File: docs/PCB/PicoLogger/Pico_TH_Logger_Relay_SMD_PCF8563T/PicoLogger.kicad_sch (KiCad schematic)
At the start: 62 parts, among them J1 Sensor, J2 LCD 16x2, J3 Additional connector, J4 K4_Output, J5 K3_Output, J6 K2_Output, J7 K1_Output, K1 G5Q-1, K2 G5Q-1, K3 G5Q-1, K4 G5Q-1, Q1 MMBT3904, Q2 MMBT3904, Q3 MMBT3904, Q4 MMBT3904, SW1 SW_Push, SW2 SW_Push, U1 LTV-817S, U2 LTV-817S, U3 LTV-817S, U4 LTV-817S, U5 PCF8563T, Y1 Crystal

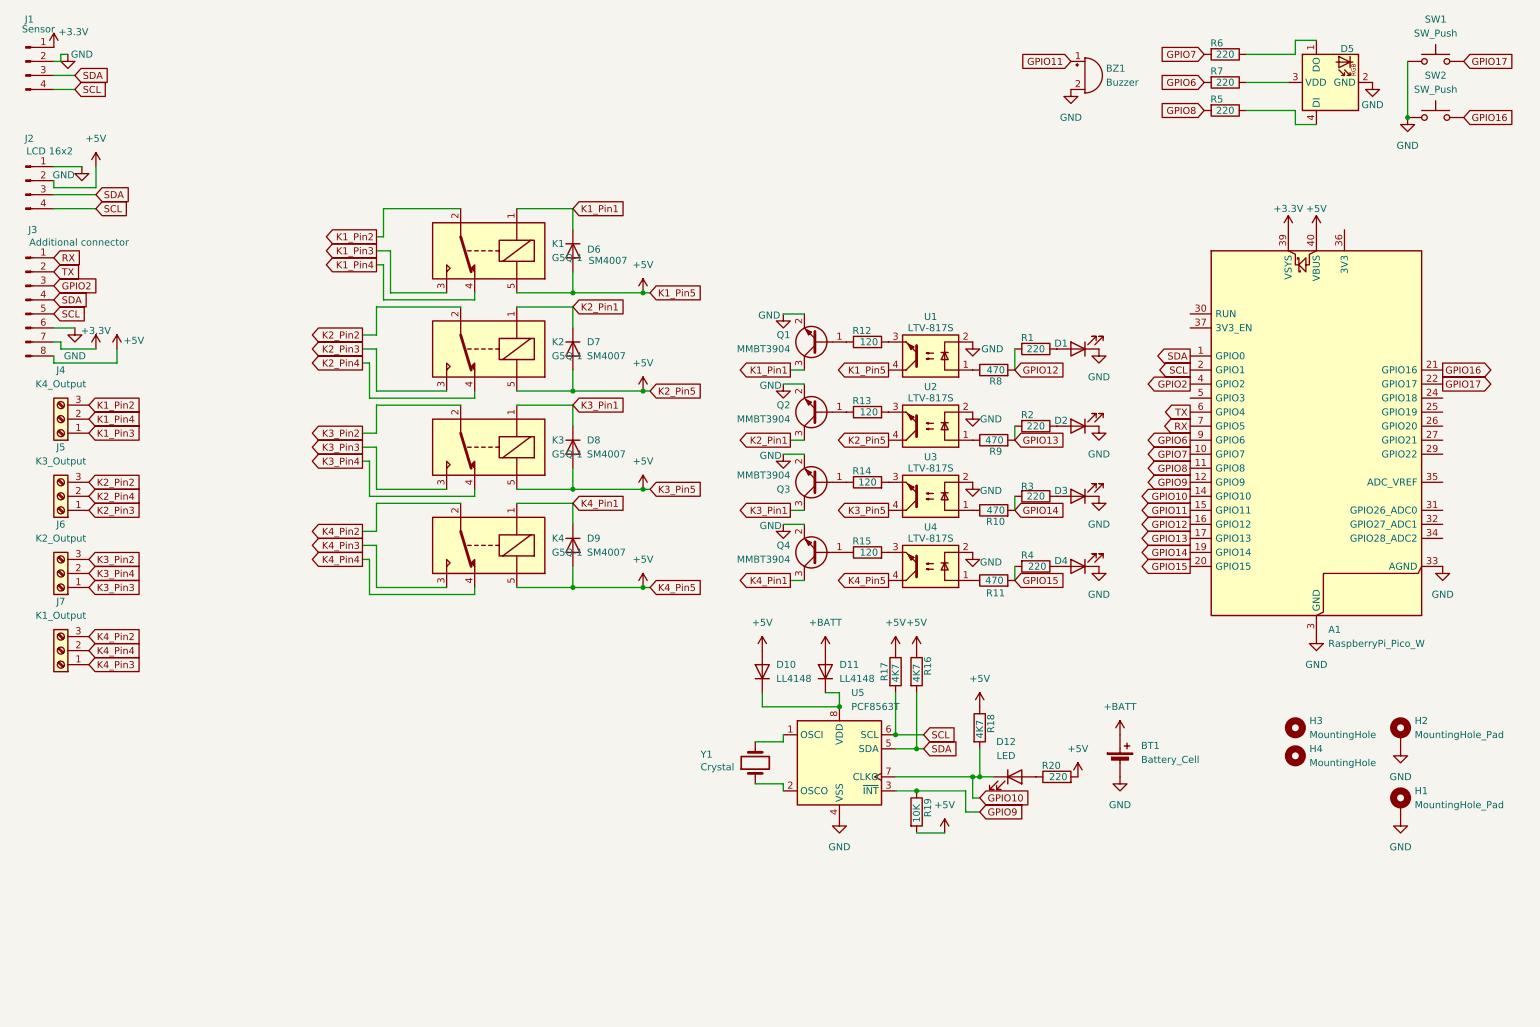
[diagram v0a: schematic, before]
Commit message: Logger docs updated.
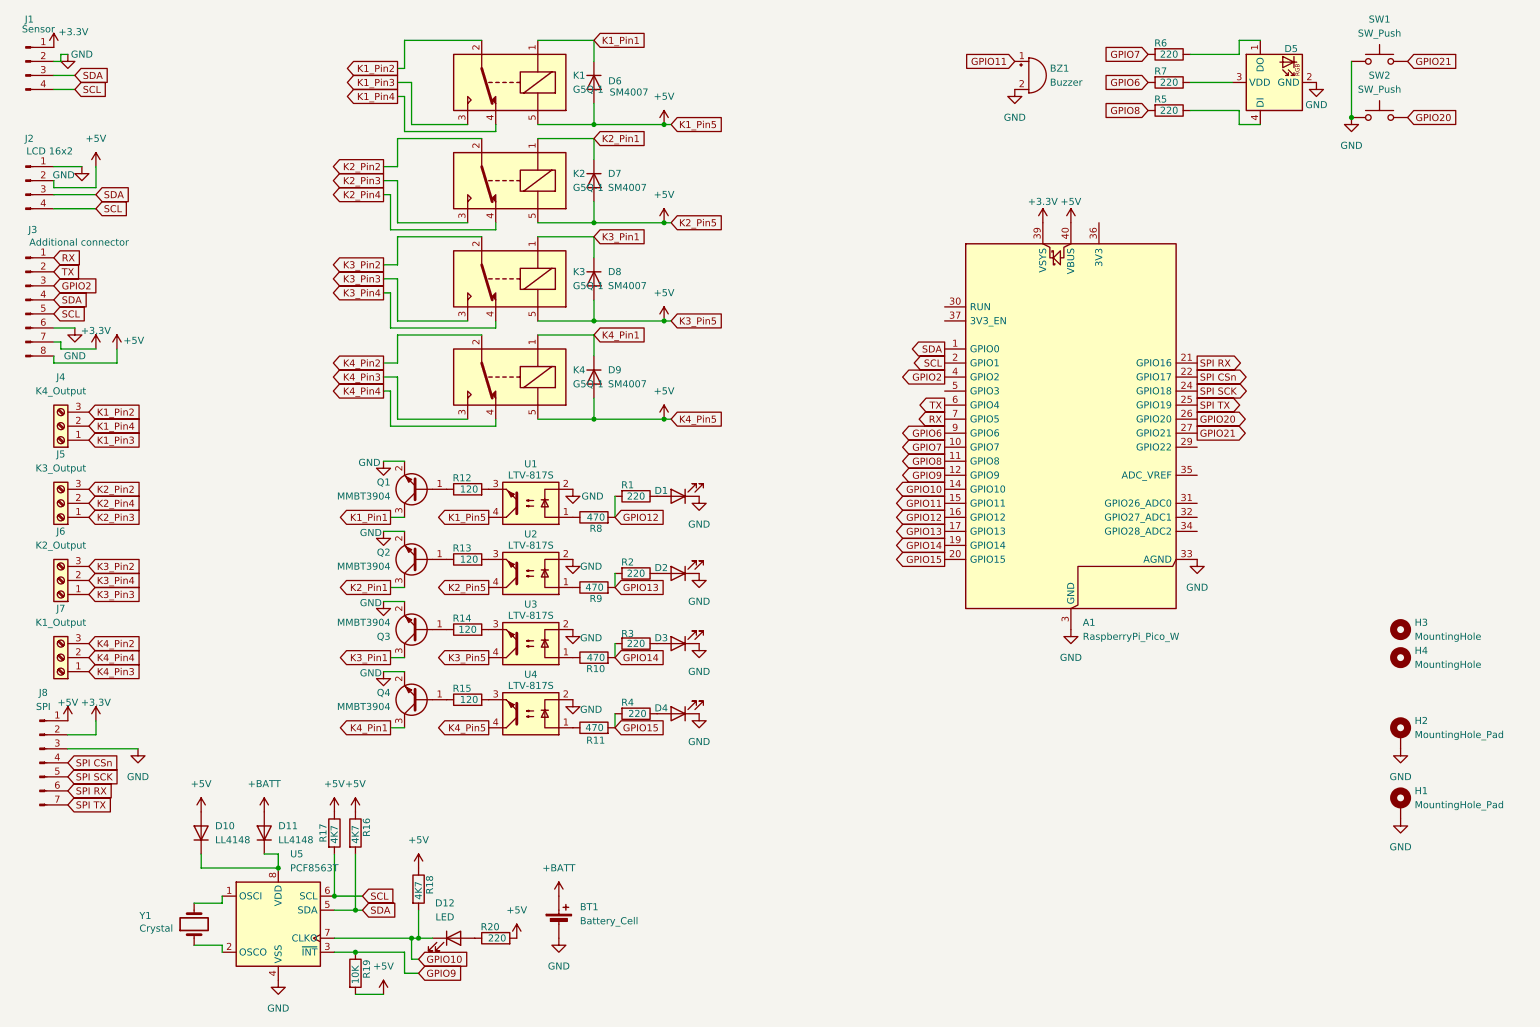
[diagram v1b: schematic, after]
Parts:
- added J8: SPI, Connector_PinHeader_2.54mm:PinHeader_1x07_P2.54mm_Horizontal, symbol Connector:Conn_01x07_Pin
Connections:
- net +3.3V: now also J8.2 (Pin_2)
- net +5V: now also J8.1 (Pin_1)
- net GND: now also J8.3 (Pin_3)
- net SPI SCK: now reaches A1.24 (GPIO18)
- net SPI SCK: now also J8.5 (Pin_5)
- net SPI TX: now reaches A1.25 (GPIO19)
- net SPI TX: now also J8.7 (Pin_7)
- net GPIO20: now reaches A1.26 (GPIO20)
- net GPIO20: now also SW2.2
- net GPIO21: now reaches A1.27 (GPIO21)
- net GPIO21: now also SW1.2
- net GPIO16 renamed SPI RX
- net SPI RX: now also J8.6 (Pin_6); no longer SW2.2
- net GPIO17 renamed SPI CSn
- net SPI CSn: now also J8.4 (Pin_4); no longer SW1.2
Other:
- company: (none) -> Creator: Piotr Kłyś
- title: (none) -> Raspberry Pi Pico Logger - Relay
- moved on the sheet: A1, BT1, BZ1, D1, D10, D11, D12, D2, D3, D4, D5, D6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

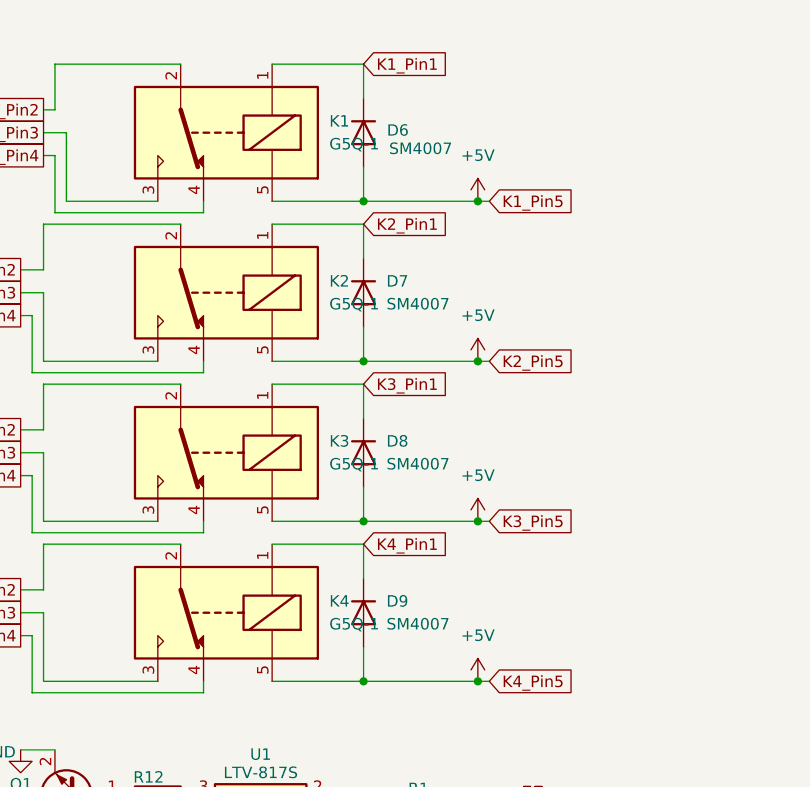
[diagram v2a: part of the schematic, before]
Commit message: Pico1 and Pico2 devices code implemented.
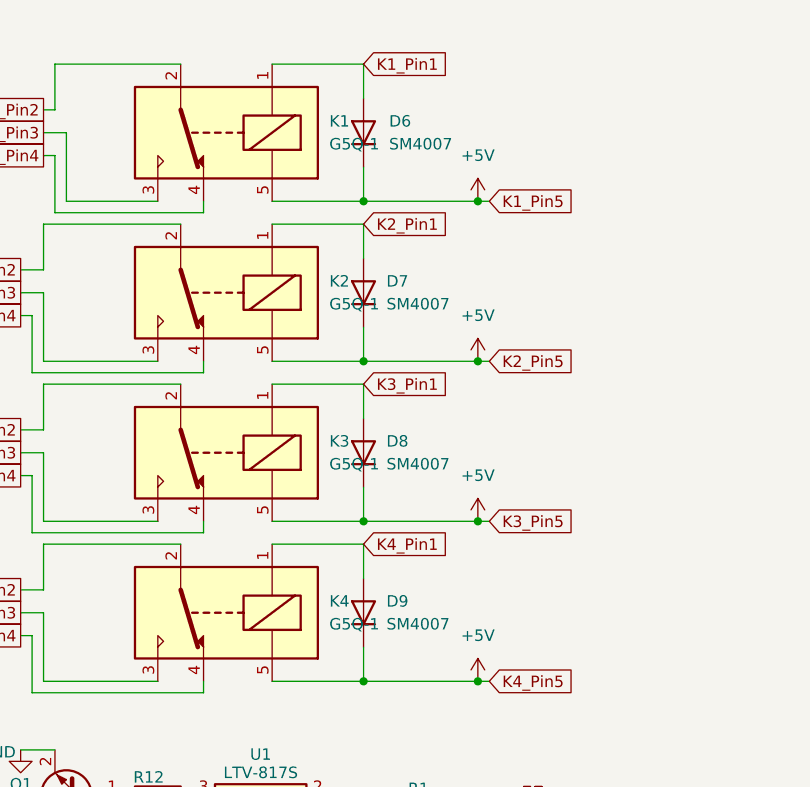
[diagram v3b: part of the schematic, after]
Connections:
- net +5V: now also D6.1 (K), D7.1 (K), D8.1 (K), D9.1 (K); no longer D6.2 (A), D7.2 (A), D8.2 (A), D9.2 (A)
- net K1_Pin1: now also D6.2 (A); no longer D6.1 (K)
- net K2_Pin1: now also D7.2 (A); no longer D7.1 (K)
- net K3_Pin1: now also D8.2 (A); no longer D8.1 (K)
- net K4_Pin1: now also D9.2 (A); no longer D9.1 (K)
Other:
- moved on the sheet: D6, D7, D8, D9
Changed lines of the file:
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@@
 	)
 	(junction
-		(at 118.11 68.58)
+		(at 118.11 86.36)
 		(diameter 0)
 		(color 0 0 0 0)
@@
 	)
 	(junction
-		(at 118.11 50.8)
+		(at 118.11 68.58)
 		(diameter 0)
 		(color 0 0 0 0)
 	)
 	(junction
-		(at 118.11 86.36)
+		(at 255.27 31.75)
 		(diameter 0)
 		(color 0 0 0 0)
 	)
 	(junction
-		(at 255.27 31.75)
+		(at 71.12 172.72)
 		(diameter 0)
 		(color 0 0 0 0)
 	)
 	(junction
-		(at 71.12 172.72)
+		(at 130.81 86.36)
 		(diameter 0)
 		(color 0 0 0 0)
 	)
 	(junction
-		(at 118.11 33.02)
+		(at 130.81 50.8)
 		(diameter 0)
 		(color 0 0 0 0)
 	)
 	(junction
-		(at 130.81 86.36)
+		(at 118.11 50.8)
 		(diameter 0)
 		(color 0 0 0 0)
 	)
 	(junction
-		(at 130.81 50.8)
+		(at 118.11 33.02)
 		(diameter 0)
 		(color 0 0 0 0)
@@
 	(wire
 		(pts
-			(xy 107.95 35.56) (xy 118.11 35.56)
+			(xy 118.11 29.21) (xy 118.11 33.02)
 		)
 		(stroke
@@
 	(wire
 		(pts
-			(xy 118.11 17.78) (xy 118.11 21.59)
+			(xy 107.95 35.56) (xy 118.11 35.56)
 		)
 		(stroke
@@
 	(wire
 		(pts
-			(xy 118.11 29.21) (xy 118.11 33.02)
+			(xy 80.01 132.08) (xy 83.82 132.08)
 		)
 		(stroke
@@
 	(wire
 		(pts
-			(xy 118.11 68.58) (xy 130.81 68.58)
+			(xy 107.95 33.02) (xy 118.11 33.02)
 		)
 		(stroke
@@
 	(wire
 		(pts
-			(xy 80.01 132.08) (xy 83.82 132.08)
+			(xy 234.95 17.78) (xy 238.76 17.78)
 		)
 		(stroke
@@
 	(wire
 		(pts
-			(xy 107.95 33.02) (xy 118.11 33.02)
+			(xy 118.11 50.8) (xy 130.81 50.8)
 		)
 		(stroke
@@
 	(wire
 		(pts
-			(xy 234.95 17.78) (xy 238.76 17.78)
+			(xy 100.33 87.63) (xy 81.28 87.63)
 		)
 		(stroke
@@
 	(wire
 		(pts
-			(xy 100.33 87.63) (xy 81.28 87.63)
+			(xy 118.11 86.36) (xy 130.81 86.36)
 		)
 		(stroke
@@
 	(wire
 		(pts
-			(xy 118.11 53.34) (xy 118.11 57.15)
+			(xy 21.59 73.66) (xy 21.59 72.39)
 		)
 		(stroke
@@
 	(wire
 		(pts
-			(xy 21.59 73.66) (xy 21.59 72.39)
+			(xy 71.12 180.34) (xy 85.09 180.34)
 		)
 		(stroke
@@
 	(wire
 		(pts
-			(xy 71.12 180.34) (xy 85.09 180.34)
+			(xy 118.11 46.99) (xy 118.11 50.8)
+		)
+		(stroke
+			(width 0)
+			(type default)
+		)
+	)
+	(wire
+		(pts
+			(xy 118.11 82.55) (xy 118.11 86.36)
 		)
 		(stroke
@@
 	(wire
 		(pts
-			(xy 74.93 175.26) (xy 76.2 175.26)
+			(xy 118.11 35.56) (xy 118.11 39.37)
 		)
 		(stroke
@@
 	(wire
 		(pts
-			(xy 121.92 127) (xy 121.92 129.54)
+			(xy 118.11 17.78) (xy 118.11 21.59)
 		)
 		(stroke
@@
 	(wire
 		(pts
-			(xy 83.82 17.78) (xy 97.79 17.78)
+			(xy 74.93 175.26) (xy 76.2 175.26)
 		)
 		(stroke
@@
 	(wire
 		(pts
-			(xy 27.94 73.66) (xy 21.59 73.66)
+			(xy 121.92 127) (xy 121.92 129.54)
 		)
 		(stroke
@@
 	(wire
 		(pts
-			(xy 20.32 72.39) (xy 21.59 72.39)
+			(xy 83.82 17.78) (xy 97.79 17.78)
 		)
 		(stroke
@@
 	(wire
 		(pts
-			(xy 74.93 190.5) (xy 80.01 190.5)
+			(xy 27.94 73.66) (xy 21.59 73.66)
 		)
 		(stroke
@@
 	(wire
 		(pts
-			(xy 107.95 50.8) (xy 118.11 50.8)
+			(xy 20.32 72.39) (xy 21.59 72.39)
 		)
 		(stroke
@@
 	(wire
 		(pts
-			(xy 118.11 82.55) (xy 118.11 86.36)
+			(xy 74.93 190.5) (xy 80.01 190.5)
 		)
 		(stroke
@@
 	(wire
 		(pts
-			(xy 82.55 86.36) (xy 95.25 86.36)
+			(xy 118.11 64.77) (xy 118.11 68.58)
 		)
 		(stroke
@@
 	(wire
 		(pts
-			(xy 118.11 35.56) (xy 118.11 39.37)
+			(xy 82.55 86.36) (xy 95.25 86.36)
 		)
 		(stroke
@@
 	(wire
 		(pts
-			(xy 118.11 33.02) (xy 130.81 33.02)
-		)
-		(stroke
-			(width 0)
-			(type default)
-		)
-	)
-	(wire
-		(pts
 			(xy 46.99 165.1) (xy 46.99 167.64)
 		)
@@
 	(wire
 		(pts
-			(xy 20.32 69.85) (xy 24.13 69.85)
+			(xy 118.11 71.12) (xy 118.11 74.93)
 		)
 		(stroke
@@
 	(wire
 		(pts
-			(xy 82.55 53.34) (xy 97.79 53.34)
+			(xy 20.32 69.85) (xy 24.13 69.85)
 		)
 		(stroke
@@
 	(wire
 		(pts
-			(xy 118.11 71.12) (xy 118.11 74.93)
+			(xy 82.55 53.34) (xy 97.79 53.34)
 		)
 		(stroke
@@
 	(wire
 		(pts
+			(xy 118.11 33.02) (xy 130.81 33.02)
+		)
+		(stroke
+			(width 0)
+			(type default)
+		)
+	)
+	(wire
+		(pts
 			(xy 86.36 186.69) (xy 83.82 186.69)
 		)
@@
 	(wire
 		(pts
-			(xy 83.82 182.88) (xy 74.93 182.88)
+			(xy 118.11 68.58) (xy 130.81 68.58)
 		)
 		(stroke
@@
 	(wire
 		(pts
-			(xy 118.11 64.77) (xy 118.11 68.58)
+			(xy 118.11 53.34) (xy 118.11 57.15)
 		)
 		(stroke
@@
 	(wire
 		(pts
-			(xy 83.82 27.94) (xy 82.55 27.94)
+			(xy 83.82 182.88) (xy 74.93 182.88)
 		)
 		(stroke
@@
 	(wire
 		(pts
-			(xy 82.55 58.42) (xy 80.01 58.42)
+			(xy 83.82 27.94) (xy 82.55 27.94)
 		)
 		(stroke
@@
 	(wire
 		(pts
-			(xy 80.01 60.96) (xy 82.55 60.96)
+			(xy 82.55 58.42) (xy 80.01 58.42)
 		)
 		(stroke
@@
 	(wire
 		(pts
-			(xy 118.11 46.99) (xy 118.11 50.8)
+			(xy 80.01 60.96) (xy 82.55 60.96)
 		)
 		(stroke
@@
 	(wire
 		(pts
-			(xy 118.11 50.8) (xy 130.81 50.8)
+			(xy 107.95 50.8) (xy 118.11 50.8)
 		)
 		(stroke
@@
 	(wire
 		(pts
-			(xy 118.11 86.36) (xy 130.81 86.36)
-		)
-		(stroke
-			(width 0)
-			(type default)
-		)
-	)
-	(wire
-		(pts
 			(xy 107.95 86.36) (xy 118.11 86.36)
 		)
@@
 	(symbol
 		(lib_id "Diode:SM4007")
-		(at 118.11 78.74 270)
+		(at 118.11 78.74 90)
 		(unit 1)
 		(exclude_from_sim no)
@@
 					(size 1.27 1.27)
 				)
-				(justify left)
+				(justify right)
 			)
 		)
@@
 					(size 1.27 1.27)
 				)
-				(justify left)
+				(justify right)
 			)
 		)
 		(property "Footprint" "Diode_SMD:D_SMA"
-			(at 113.665 78.74 0)
+			(at 122.555 78.74 0)
 			(effects
 				(font
@@
 	(symbol
 		(lib_id "Diode:SM4007")
-		(at 118.11 25.4 270)
+		(at 118.11 25.4 90)
 		(unit 1)
 		(exclude_from_sim no)
@@
 		(dnp no)
 		(property "Reference" "D6"
-			(at 121.92 25.146 90)
+			(at 122.174 24.13 90)
 			(effects
 				(font
@@
 		)
 		(property "Value" "SM4007"
-			(at 124.46 27.178 90)
+			(at 124.46 26.67 90)
 			(effects
 				(font
@@
 		)
 		(property "Footprint" "Diode_SMD:D_SMA"
-			(at 113.665 25.4 0)
+			(at 122.555 25.4 0)
 			(effects
 				(font
@@
 		(on_board yes)
 		(dnp no)
-		(fields_autoplaced yes)
 		(property "Reference" "K3"
 			(at 114.3 59.6899 0)
@@
 		(on_board yes)
 		(dnp no)
-		(fields_autoplaced yes)
 		(property "Reference" "K4"
 			(at 114.3 77.4699 0)
@@
 	(symbol
 		(lib_id "Diode:SM4007")
-		(at 118.11 60.96 270)
+		(at 118.11 60.96 90)
 		(unit 1)
 		(exclude_from_sim no)
@@
 					(size 1.27 1.27)
 				)
-				(justify left)
+				(justify right)
 			)
 		)
@@
 					(size 1.27 1.27)
 				)
-				(justify left)
+				(justify right)
 			)
 		)
 		(property "Footprint" "Diode_SMD:D_SMA"
-			(at 113.665 60.96 0)
+			(at 122.555 60.96 0)
 			(effects
 				(font
@@
 		(on_board yes)
 		(dnp no)
-		(fields_autoplaced yes)
 		(property "Reference" "K1"
 			(at 114.3 24.1299 0)
@@
 	(symbol
 		(lib_id "Diode:SM4007")
-		(at 118.11 43.18 270)
+		(at 118.11 43.18 90)
 		(unit 1)
 		(exclude_from_sim no)
@@
 					(size 1.27 1.27)
 				)
-				(justify left)
+				(justify right)
 			)
 		)
@@
 					(size 1.27 1.27)
 				)
-				(justify left)
+				(justify right)
 			)
 		)
 		(property "Footprint" "Diode_SMD:D_SMA"
-			(at 113.665 43.18 0)
+			(at 122.555 43.18 0)
 			(effects
 				(font

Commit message: Updated docs.
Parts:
- removed BT1: Battery_Cell, Battery:BatteryHolder_Keystone_104_1x23mm, symbol Device:Battery_Cell
- removed BZ1: Buzzer, Buzzer_Beeper:Buzzer_12x9.5RM7.6, symbol Device:Buzzer
- removed D1, D12, D2, D3, D4: LED, LED_SMD:LED_0805_2012Metric, symbol Device:LED
- removed D10, D11: LL4148, Diode_SMD:D_MiniMELF, symbol Diode:LL4148
- removed D5: APA-106-F5, LED_SMD:LED_Avago_PLCC4_3.2x2.8mm_CW, symbol LED:APA-106-F5
- removed D6, D7, D8, D9: SM4007, Diode_SMD:D_SMA, symbol Diode:SM4007
- removed J1: Sensor, Connector_PinHeader_2.54mm:PinHeader_1x04_P2.54mm_Vertical, symbol Connector:Conn_01x04_Pin
- removed J2: LCD 16x2, Connector_PinHeader_2.54mm:PinHeader_1x04_P2.54mm_Vertical, symbol Connector:Conn_01x04_Pin
- removed J3: Additional connector, Connector_PinHeader_2.54mm:PinHeader_1x08_P2.54mm_Horizontal, symbol Connector:Conn_01x08_Pin
- removed J4: K4_Output, TerminalBlock_Phoenix:TerminalBlock_Phoenix_MKDS-1,5-3_1x03_P5.00mm_Horizontal, symbol Connector:Screw_Terminal_01x03
- removed J5: K3_Output, TerminalBlock_Phoenix:TerminalBlock_Phoenix_MKDS-1,5-3_1x03_P5.00mm_Horizontal, symbol Connector:Screw_Terminal_01x03
- removed J6: K2_Output, TerminalBlock_Phoenix:TerminalBlock_Phoenix_MKDS-1,5-3_1x03_P5.00mm_Horizontal, symbol Connector:Screw_Terminal_01x03
- removed J7: K1_Output, TerminalBlock_Phoenix:TerminalBlock_Phoenix_MKDS-1,5-3_1x03_P5.00mm_Horizontal, symbol Connector:Screw_Terminal_01x03
- removed J8: SPI, Connector_PinHeader_2.54mm:PinHeader_1x07_P2.54mm_Horizontal, symbol Connector:Conn_01x07_Pin
- removed K1, K2, K3, K4: G5Q-1, Relay_THT:Relay_SPDT_Omron-G5Q-1, symbol Relay:G5Q-1
- removed Q1, Q2, Q3, Q4: MMBT3904, Package_TO_SOT_SMD:SOT-23, symbol Transistor_BJT:MMBT3904
- removed R1, R2, R20, R3, R4, R5, R6, R7: 220, Resistor_SMD:R_0805_2012Metric, symbol Device:R
- removed R10, R11, R8, R9: 470, Resistor_SMD:R_0805_2012Metric, symbol Device:R
- removed R12, R13, R14, R15: 120, Resistor_SMD:R_0805_2012Metric, symbol Device:R
- removed R16, R17, R18: 4K7, Resistor_SMD:R_0805_2012Metric, symbol Device:R
- removed R19: 10K, Resistor_SMD:R_0805_2012Metric, symbol Device:R
- removed SW1, SW2: SW_Push, Button_Switch_THT:SW_PUSH_6mm, symbol Switch:SW_Push
- removed U1, U2, U3, U4: LTV-817S, Package_DIP:SMDIP-4_W9.53mm, symbol Isolator:LTV-817S
- removed U5: PCF8563T, Package_SO:SOIC-8_3.9x4.9mm_P1.27mm, symbol Timer_RTC:PCF8563T
- removed Y1: Crystal, Crystal:Crystal_SMD_3215-2Pin_3.2x1.5mm, symbol Device:Crystal
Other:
- added sheet connectors (connectors.kicad_sch)
- added sheet isolation_relays (isolation_relays.kicad_sch)
- added sheet peripherals (peripherals.kicad_sch)
- added sheet relays (relays.kicad_sch)
- added sheet rtc (rtc.kicad_sch)
- moved on the sheet: A1, H1, H2, H3, H4
